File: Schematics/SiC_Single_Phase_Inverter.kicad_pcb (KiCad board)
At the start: 2 copper layers, 18 parts

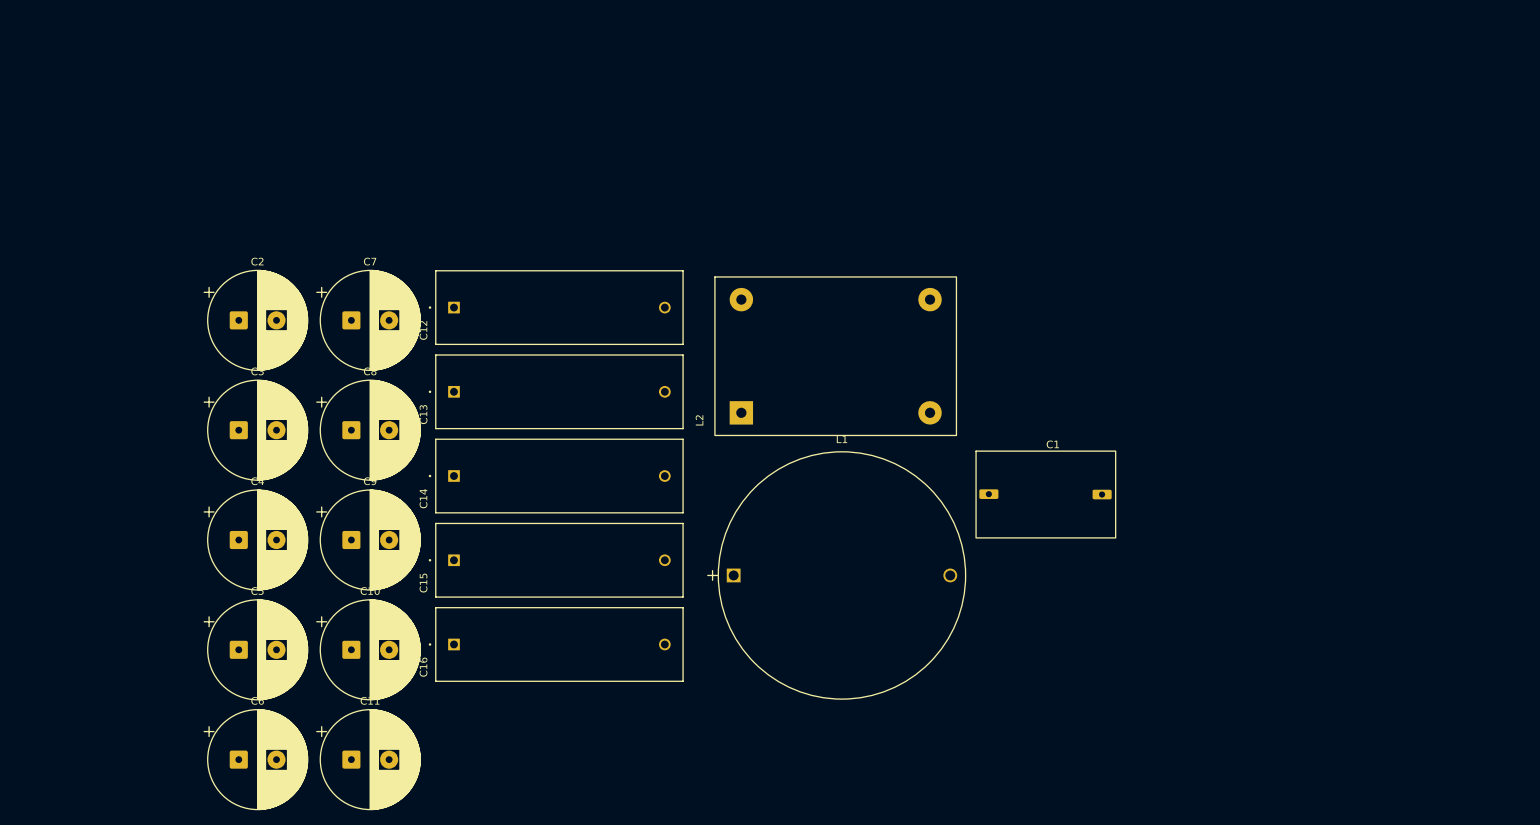
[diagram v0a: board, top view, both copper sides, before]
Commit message: [SiC Inverter WIP]
- Deleted backup files
- changed symbol and footprint lib locations
- added text discription explaining the DC link sub sheet and emi  input
  filter subsheet
- Added Vin+,- Black and Red connector
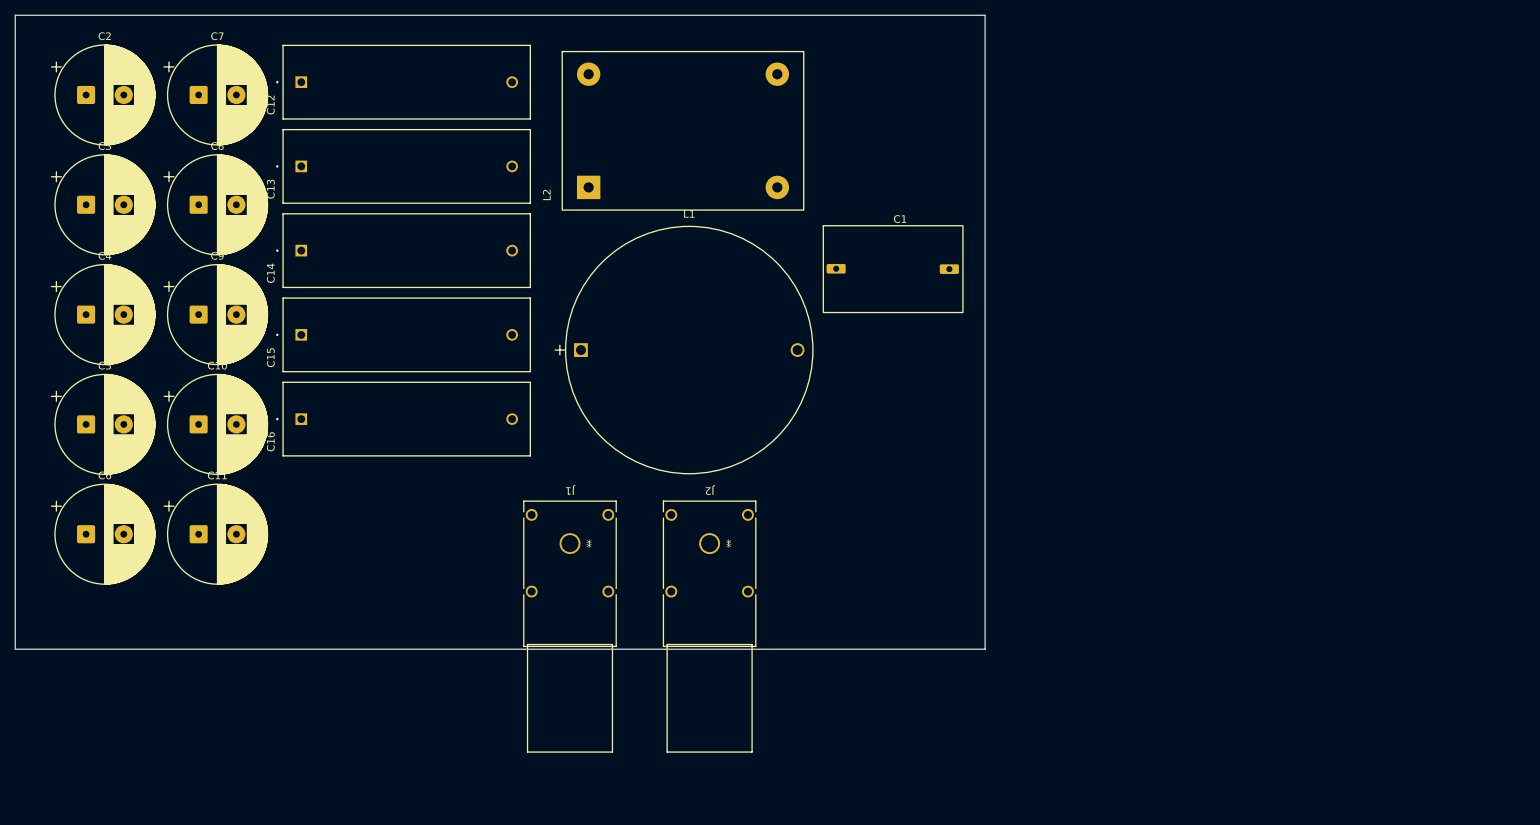
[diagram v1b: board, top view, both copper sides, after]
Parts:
- added J1: 23AH8785-Black, SiC_Inverter:23AH8785-Black, F.Cu at (143.5, 107.5)
- added J2: 23AH8786-Red, SiC_Inverter:23AH8786-Red, F.Cu at (162.0, 107.5)
- moved C4 36.1 mm to (79.4, 77.2)
- moved C9 36.1 mm to (94.3, 77.2)
- moved L1 36.1 mm to (145.0, 81.9)
- moved C16 36.1 mm to (107.9, 91.0)
- moved C1 36.1 mm to (177.1, 76.9)
- moved C10 36.1 mm to (94.3, 91.7)
- moved C11 36.1 mm to (94.3, 106.3)
- moved C12 36.1 mm to (107.9, 46.4)
- moved C13 36.1 mm to (107.9, 57.5)
- moved C2 36.1 mm to (79.4, 48.1)
- moved C3 36.1 mm to (79.4, 62.6)
- moved C5 36.1 mm to (79.4, 91.7)
- moved C6 36.1 mm to (79.4, 106.3)
- moved C7 36.1 mm to (94.3, 48.1)
- moved C8 36.1 mm to (94.3, 62.6)
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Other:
- board outline added: 128.5 x 84 mm

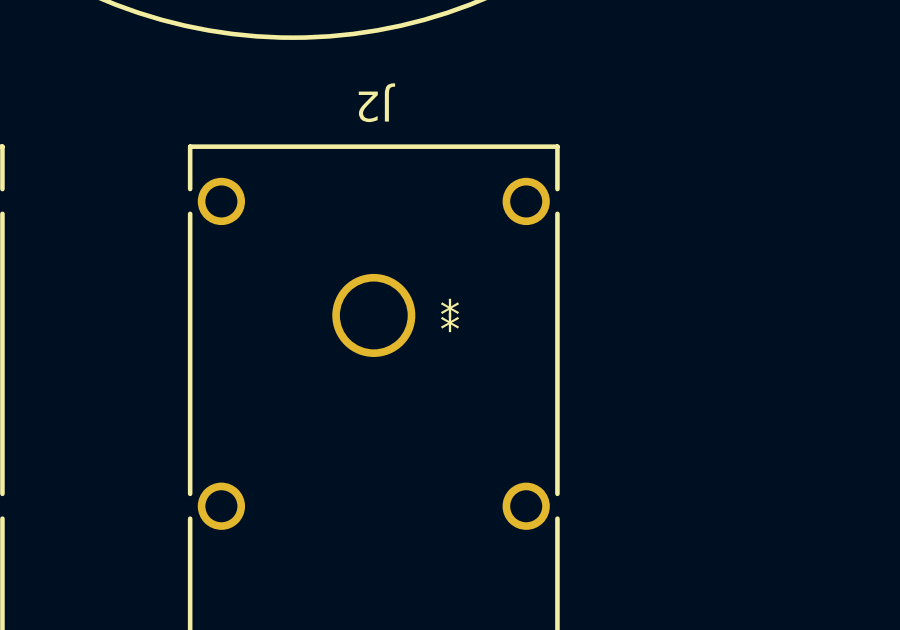
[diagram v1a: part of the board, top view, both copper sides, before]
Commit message: Added 3d models for connectors and caps
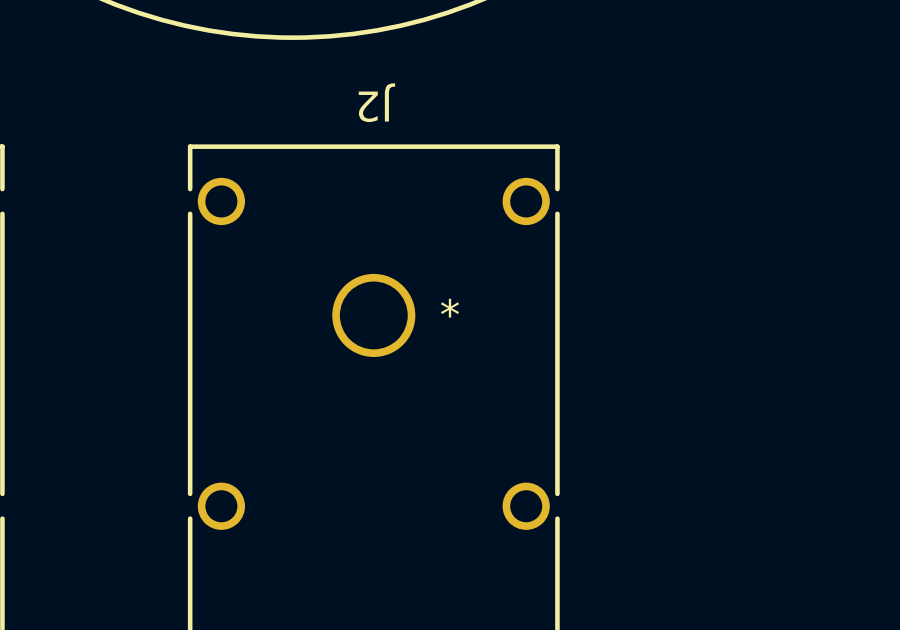
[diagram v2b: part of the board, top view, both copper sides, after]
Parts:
- J1: value 23AH8785-Black -> CONN_66.9040-21_MTC
- J2: value 23AH8786-Red -> CONN_66.9040-21_MTC
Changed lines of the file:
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@@
 		)
 		(embedded_fonts no)
+		(model "${KIPRJMOD}/3d-models/MKP1848C52050JK2.step"
+			(offset
+				(xyz -2 -4.5 0)
+			)
+			(scale
+				(xyz 1 1 1)
+			)
+			(rotate
+				(xyz -0 -0 -0)
+			)
+		)
 	)
 	(footprint "SiC_Inverter:MKP1848C52050JK2"
@@
 		)
 		(embedded_fonts no)
+		(model "${KIPRJMOD}/3d-models/MKP1848C52050JK2.step"
+			(offset
+				(xyz -2 -4.5 0)
+			)
+			(scale
+				(xyz 1 1 1)
+			)
+			(rotate
+				(xyz -0 -0 -0)
+			)
+		)
 	)
 	(footprint "SiC_Inverter:7448258022"
@@
 			)
 		)
-		(property "Value" "23AH8785-Black"
+		(property "Value" "CONN_66.9040-21_MTC"
 			(at 13 7 180)
 			(unlocked yes)
@@
 		)
 		(fp_text user "*"
-			(at -2.54 0 0)
+			(at -2.54 0 180)
+			(unlocked yes)
 			(layer "F.SilkS")
 			(effects
@@
 		(fp_text user "*"
 			(at -2.54 0 180)
-			(unlocked yes)
 			(layer "F.SilkS")
 			(effects
@@
 		)
 		(fp_text user "*"
-			(at -2.54 0 0)
+			(at -2.54 0 180)
+			(unlocked yes)
 			(layer "F.Fab")
 			(effects
@@
 		)
 		(embedded_fonts no)
-		(model "${KIPRJMOD}/3d-models/23AH8785_Black.stp"
+		(model "${KIPRJMOD}/3d-models/66.9040-21_Black.stp"
 			(offset
 				(xyz 0 27.5 5.5)
@@
 			)
 		)
-		(property "Value" "23AH8786-Red"
+		(property "Value" "CONN_66.9040-21_MTC"
 			(at 13 7 180)
 			(unlocked yes)
@@
 		(fp_text user "*"
 			(at -2.54 0 180)
-			(unlocked yes)
 			(layer "F.SilkS")
 			(effects
@@
 			)
 		)
-		(fp_text user "${REFERENCE}"
-			(at 10 9 180)
+		(fp_text user "*"
+			(at -2.54 0 180)
 			(unlocked yes)
 			(layer "F.Fab")
@@
 			)
 		)
-		(fp_text user "*"
-			(at -2.54 0 180)
+		(fp_text user "${REFERENCE}"
+			(at 10 9 180)
 			(unlocked yes)
 			(layer "F.Fab")
@@
 		)
 		(embedded_fonts no)
+		(model "${KIPRJMOD}/3d-models/66.9040-22_Red.stp"
+			(offset
+				(xyz 0 27.5 5.5)
+			)
+			(scale
+				(xyz 1 1 1)
+			)
+			(rotate
+				(xyz -180 -180 -0)
+			)
+		)
 	)
 	(footprint "SiC_Inverter:ESH226M500AL4AA"
@@
 		)
 		(embedded_fonts no)
+		(model "${KIPRJMOD}/3d-models/R71P1410050H6K.step"
+			(offset
+				(xyz 0 0 0)
+			)
+			(scale
+				(xyz 1 1 1)
+			)
+			(rotate
+				(xyz -0 -0 -0)
+			)
+		)
 	)
 	(footprint "SiC_Inverter:ESH226M500AL4AA"
@@
 		)
 		(embedded_fonts no)
+		(model "${KIPRJMOD}/3d-models/MKP1848C52050JK2.step"
+			(offset
+				(xyz -2 -4.5 0)
+			)
+			(scale
+				(xyz 1 1 1)
+			)
+			(rotate
+				(xyz -0 -0 -0)
+			)
+		)
 	)
 	(footprint "SiC_Inverter:ESH226M500AL4AA"
@@
 		)
 		(embedded_fonts no)
+		(model "${KIPRJMOD}/3d-models/MKP1848C52050JK2.step"
+			(offset
+				(xyz -2 -4.5 0)
+			)
+			(scale
+				(xyz 1 1 1)
+			)
+			(rotate
+				(xyz -0 -0 -0)
+			)
+		)
 	)
 	(footprint "SiC_Inverter:ESH226M500AL4AA"
@@
 		)
 		(embedded_fonts no)
+		(model "${KIPRJMOD}/3d-models/MKP1848C52050JK2.step"
+			(offset
+				(xyz -2 -4.5 0)
+			)
+			(scale
+				(xyz 1 1 1)
+			)
+			(rotate
+				(xyz -0 -0 -0)
+			)
+		)
 	)
 	(footprint "SiC_Inverter:2300HT_470"

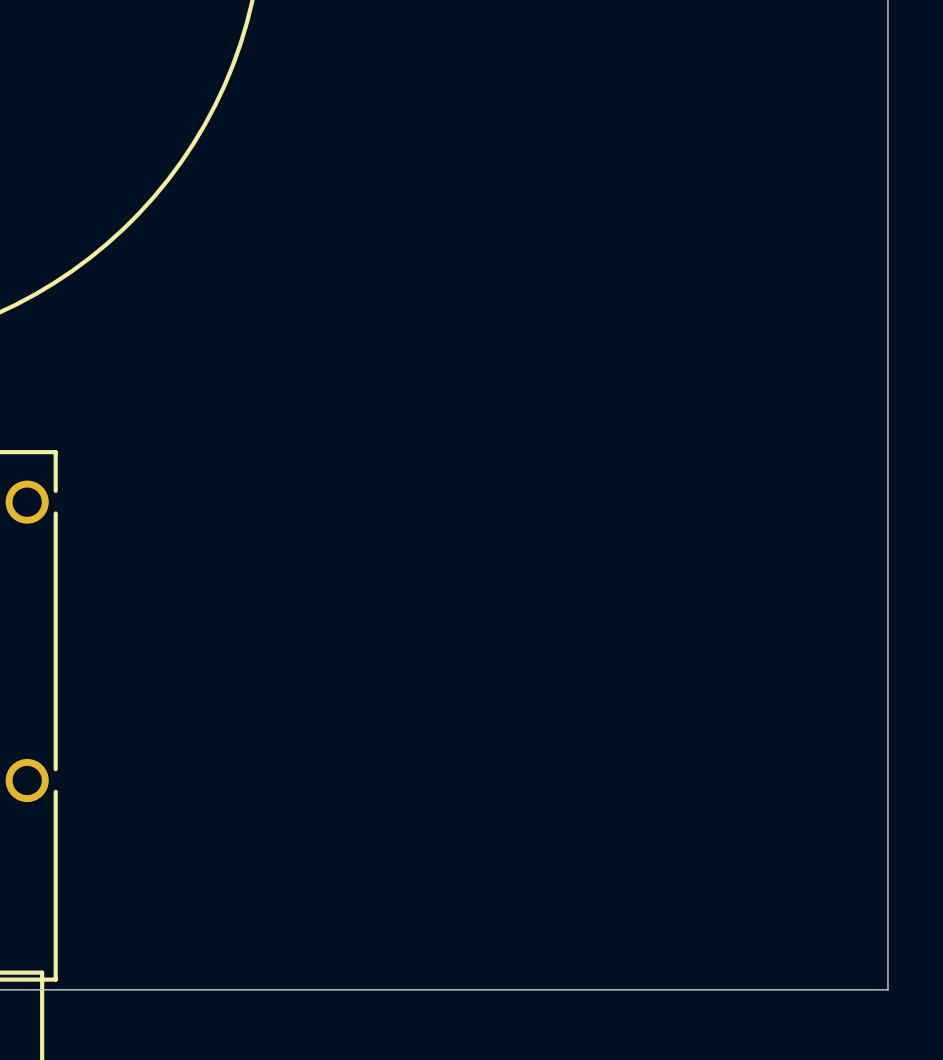
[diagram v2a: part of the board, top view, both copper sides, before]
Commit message: Work in progress
- Added new parts to PCB to check 3d models
- Added input protection sheet
- Added TVS, N-Channel MOSFET, Zensor, and resiters to protection
  circuit
- Added datasheets for new parts
- Added circuit GND
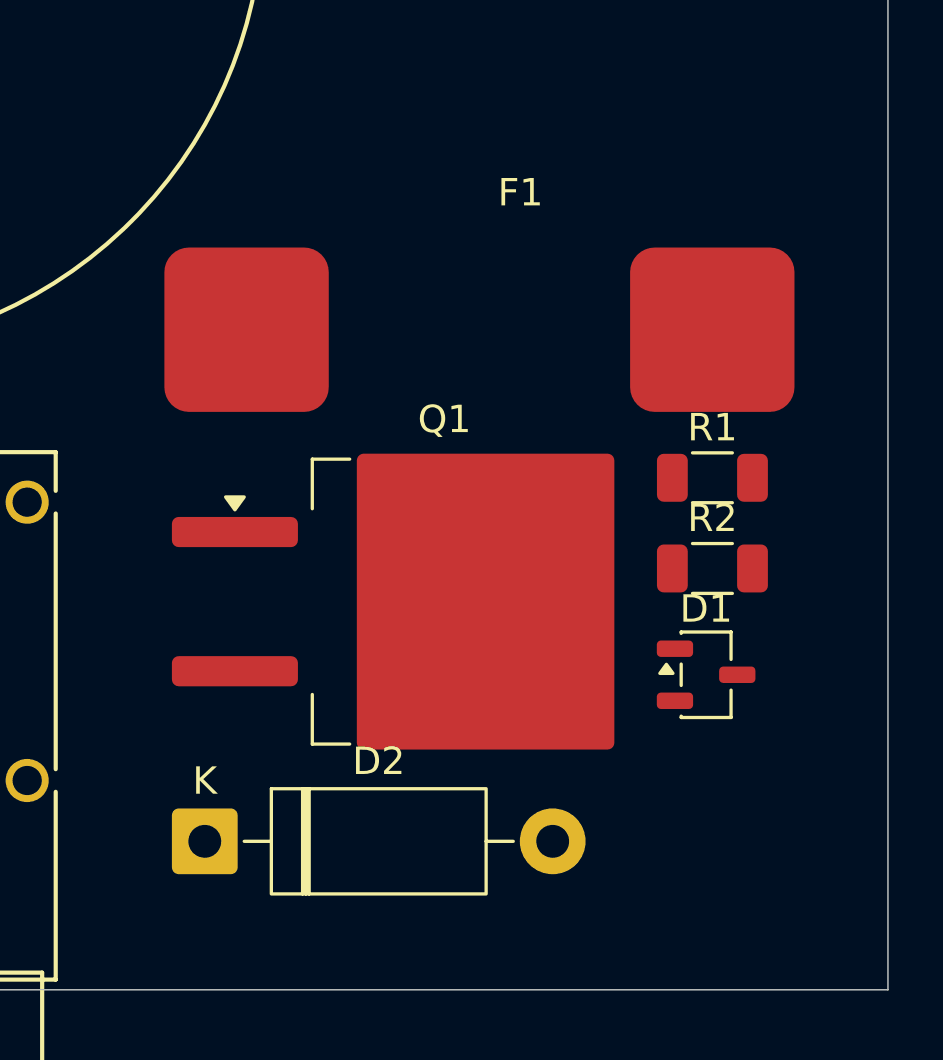
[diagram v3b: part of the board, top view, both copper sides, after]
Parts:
- added D1: BZX84C15-7-F, Package_TO_SOT_SMD:SOT-23-3, F.Cu at (191.9, 110.0)
- added D2: P6KE500A-HF, Diode_THT:D_DO-15_P12.70mm_Horizontal, F.Cu at (173.6, 116.1)
- added F1: 0031.8322, SiC_Inverter:0031.8322, F.Cu at (189.1, 100.4)
- added Q1: STB10NK60ZT4, Package_TO_SOT_SMD:TO-263-2, F.Cu at (182.3, 107.3)
- added R1: 100K, Resistor_SMD:R_1206_3216Metric, F.Cu at (192.1, 102.8)
- added R2: 47, Resistor_SMD:R_1206_3216Metric, F.Cu at (192.1, 106.1)
- J1: value CONN_66.9040-21_MTC -> 23AH8785-Black
- J2: value CONN_66.9040-21_MTC -> 23AH8786-Red
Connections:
- C1 pad 2: -VIN -> GND
- L1 pad 1: +VIN -> /EMI_Input_Filter/+VIN_EMI
- L2 pad 2: -VIN -> GND
